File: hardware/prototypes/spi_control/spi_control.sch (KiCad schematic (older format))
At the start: 84 parts, among them J1 USB_B_Micro, J39 Versa_1, J40 Versa_2, U1 ST1L08SPU33R, U2 MCP2210-I_MQ, U3 ADAR7251, U4 BGT24_Module, Y1 12MHZ, Y2 40MHz

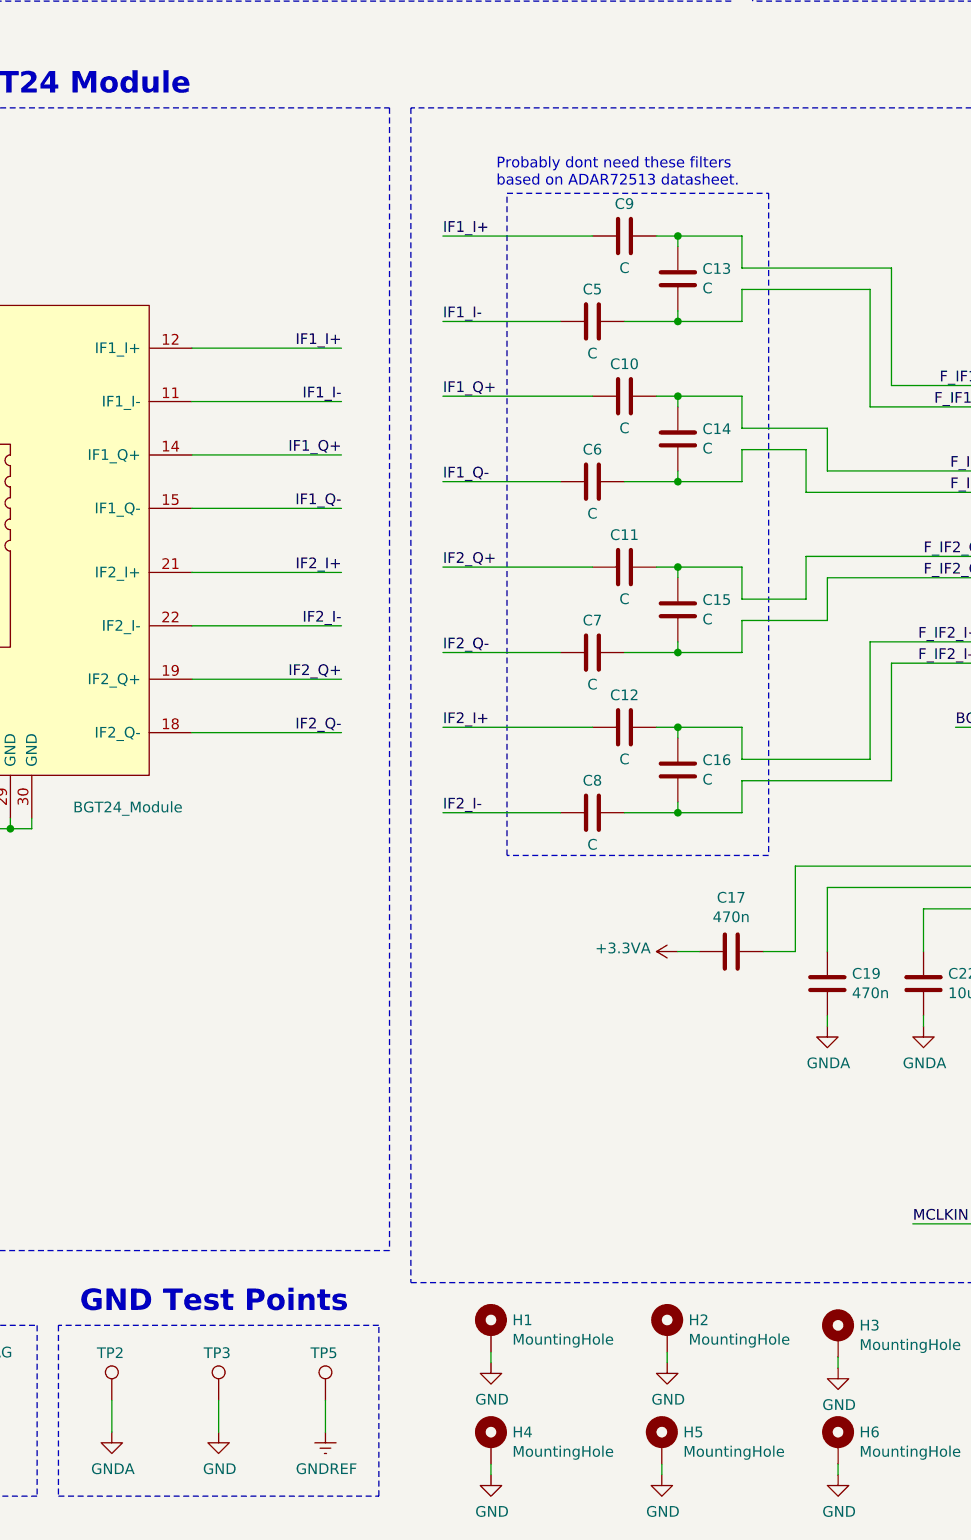
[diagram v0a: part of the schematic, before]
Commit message: Added Keystone GND probe point.
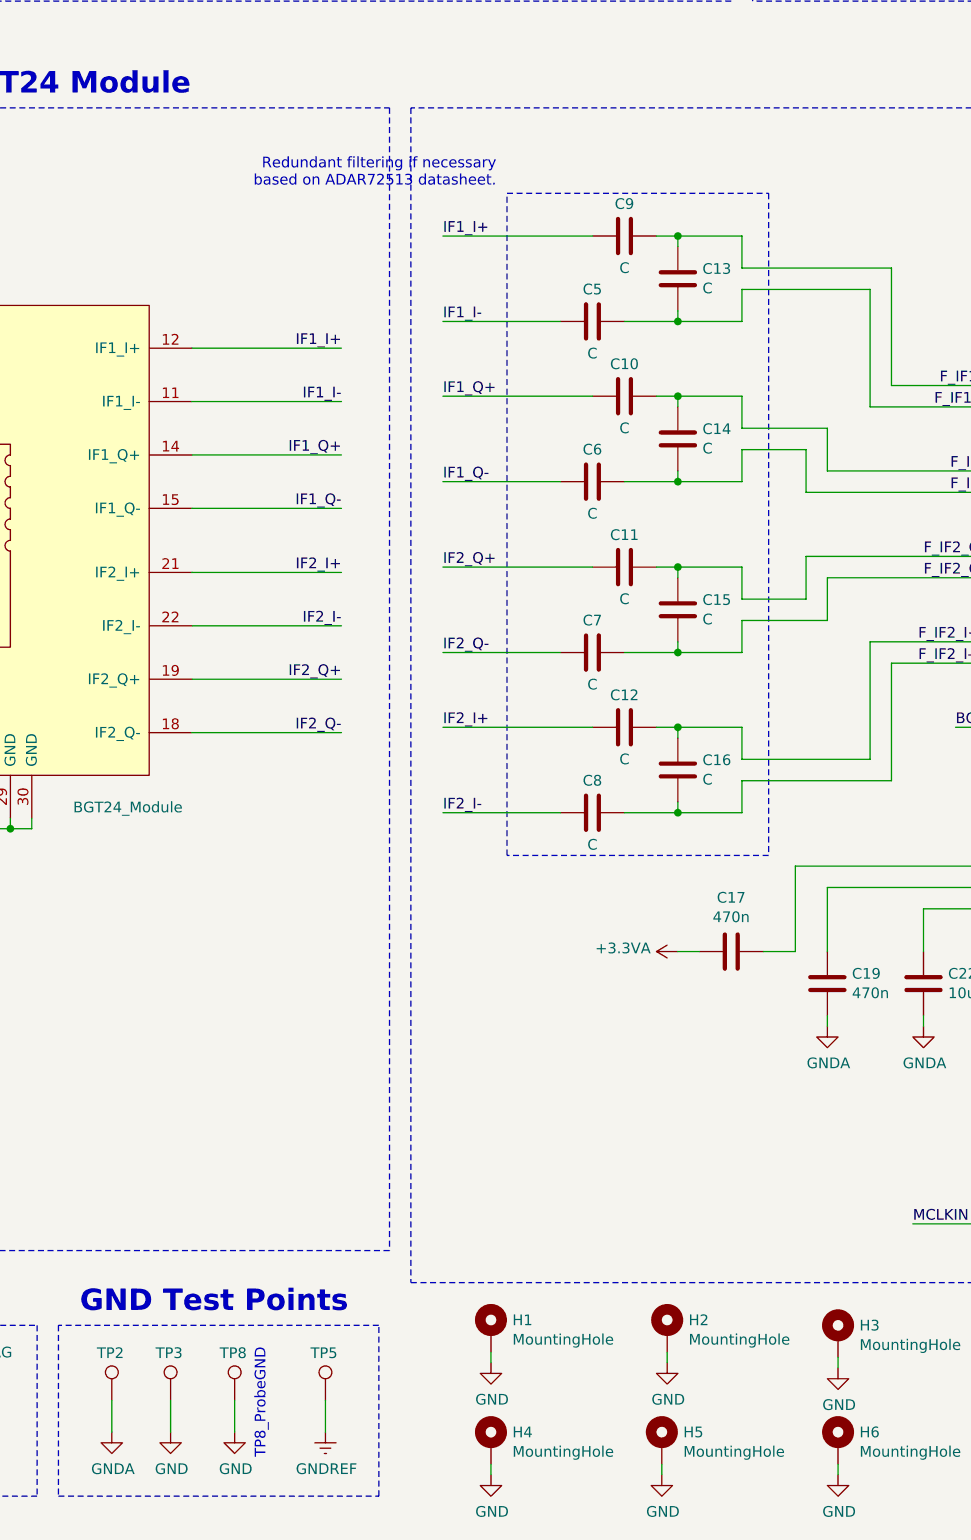
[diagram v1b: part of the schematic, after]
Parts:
- added TP8: TestPoint, TestPoint:TestPoint_Keystone_5019_Minature, symbol Connector:TestPoint
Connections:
- net GND: now also TP8.1
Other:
- note added: "Redundant filtering if necessary\nbased on ADAR72513 datasheet."
- note added: "TP8_ProbeGND"
- note removed: "Probably dont need these filters \nbased on ADAR72513 datasheet."
- moved on the sheet: TP3
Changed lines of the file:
@@
 L Connector:TestPoint TP3
 U 1 1 5E6578F5
-P 4100 9900
-F 0 "TP3" H 4030 10120 50  0000 L CNN
-F 1 "TestPoint" H 4158 9927 50  0001 L CNN
-F 2 "TestPoint:TestPoint_Pad_D1.0mm" H 4300 9900 50  0001 C CNN
-F 3 "~" H 4300 9900 50  0001 C CNN
-	1    4100 9900
+P 3875 9900
+F 0 "TP3" H 3805 10120 50  0000 L CNN
+F 1 "TestPoint" H 3933 9927 50  0001 L CNN
+F 2 "TestPoint:TestPoint_Pad_D1.0mm" H 4075 9900 50  0001 C CNN
+F 3 "~" H 4075 9900 50  0001 C CNN
+	1    3875 9900
 	1    0    0    -1
 $EndComp
@@
 L power:GND #PWR0142
 U 1 1 5E66375C
-P 4100 10050
-F 0 "#PWR0142" H 4100 9800 50  0001 C CNN
-F 1 "GND" H 4105 9877 50  0000 C CNN
-F 2 "" H 4100 10050 50  0001 C CNN
-F 3 "" H 4100 10050 50  0001 C CNN
-	1    4100 10050
+P 3875 10050
+F 0 "#PWR0142" H 3875 9800 50  0001 C CNN
+F 1 "GND" H 3880 9877 50  0000 C CNN
+F 2 "" H 3875 10050 50  0001 C CNN
+F 3 "" H 3875 10050 50  0001 C CNN
+	1    3875 10050
 	1    0    0    -1
 $EndComp
@@
 	4600 10050 4600 9900
 Wire Wire Line
-	4100 9900 4100 10050
+	3875 9900 3875 10050
 Wire Wire Line
 	3600 9900 3600 10050
@@
 Wire Notes Line
 	6675 4250 6675 7350
-Text Notes 5400 4225 0    50   ~ 0
-Probably dont need these filters \nbased on ADAR72513 datasheet.
+Text Notes 5400 4225 2    50   ~ 0
+Redundant filtering if necessary\nbased on ADAR72513 datasheet.
 Text Label 4675 6275 2    50   ~ 0
 IF2_I-
@@
 Wire Notes Line
 	5450 4250 6675 4250
+$Comp
+L Connector:TestPoint TP8
+U 1 1 5EA8B203
+P 4175 9900
+F 0 "TP8" H 4105 10120 50  0000 L CNN
+F 1 "TestPoint" H 4233 9927 50  0001 L CNN
+F 2 "TestPoint:TestPoint_Keystone_5019_Minature" H 4375 9900 50  0001 C CNN
+F 3 "~" H 4375 9900 50  0001 C CNN
+	1    4175 9900
+	1    0    0    -1
+$EndComp
+$Comp
+L power:GND #PWR?
+U 1 1 5EA8B209
+P 4175 10050
+F 0 "#PWR?" H 4175 9800 50  0001 C CNN
+F 1 "GND" H 4180 9877 50  0000 C CNN
+F 2 "" H 4175 10050 50  0001 C CNN
+F 3 "" H 4175 10050 50  0001 C CNN
+	1    4175 10050
+	1    0    0    -1
+$EndComp
+Wire Wire Line
+	4175 9900 4175 10050
+Text Notes 4325 10175 1    50   ~ 0
+TP8_ProbeGND
 $EndSCHEMATC

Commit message: Resolve 4, 11, 16, 18, and 25 from #24 and includes misc. improvements
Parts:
- added M1, M2, M3, M4, M5, M6: STANDOFF, symbol bloop:STANDOFF
- C10, C11, C12, C13, C14, C15, C16, C5, C6, C7, C8, C9: value C -> TBD
- H1, H2, H3, H4, H5, H6: value MountingHole -> MNT_HOLE
- renumbered C21 to C18, C18 to C19, C19 to C20, C20 to C21, FB2 to FB1, FB1 to FB2, J40 to J2, J39 to J3, TP8 to TP4, TP4 to TP6, TP6 to TP7, TP7 to TP8, U4 to U1, U1 to U2, U2 to U3, U3 to U4
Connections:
- net GND: now also J1.5 (GND)
- net GNDREF: no longer J1.5 (GND)
- no-connect marks 35 -> 36
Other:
- note added: "32 mA (typ)"
- note added: "M2 Standoffs"
- note added: "Mounting Holes"
- note added: "Radar MMIC - BGT24 Module"
- note removed: "RF Transceiver - BGT24 Module"
- moved on the sheet: C18, C23, C25, C26, H1, H2, H3, H4, H5, H6, R5, R6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

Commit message: Resolve 9 from #24; added some vias to layout and moved a few tracks
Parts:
- Y2: footprint Oscillator:Oscillator_SMD_Abracon_ASE-4Pin_3.2x2.5mm -> Crystal:Crystal_SMD_Abracon_ABM8G-4Pin_3.2x2.5mm
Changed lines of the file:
@@
 Wire Wire Line
 	1450 1500 2050 1500
-$Comp
-L Device:Crystal_GND24 Y1
-U 1 1 5FC6E4E6
-P 7300 2500
-F 0 "Y1" H 7400 2275 50  0000 L CNN
-F 1 "12MHZ" H 6900 2650 50  0000 L CNN
-F 2 "Crystal:Crystal_SMD_Abracon_ABM8G-4Pin_3.2x2.5mm" H 7300 2500 50  0001 C CNN
-F 3 "https://ecsxtal.com/store/pdf/ecx-32.pdf" H 7300 2500 50  0001 C CNN
-F 4 "ECS-120-12-33-AGN-TR" H 7300 2500 50  0001 C CNN "MPN"
-	1    7300 2500
-	1    0    0    -1
-$EndComp
 Connection ~ 9275 8350
 Wire Wire Line
@@
 F 0 "Y2" V 9100 8475 50  0000 L CNN
 F 1 "40MHz" V 9100 8700 50  0000 L CNN
-F 2 "Oscillator:Oscillator_SMD_Abracon_ASE-4Pin_3.2x2.5mm" H 9275 8625 50  0001 C CNN
+F 2 "Crystal:Crystal_SMD_Abracon_ABM8G-4Pin_3.2x2.5mm" H 9275 8625 50  0001 C CNN
 F 3 "https://ecsxtal.com/store/pdf/ecx-32.pdf" H 9275 8625 50  0001 C CNN
 F 4 "ECS-400-18-33-JGN-TR" H 9275 8625 50  0001 C CNN "MPN"
@@
 Wire Wire Line
 	7250 1250 7250 1300
+$Comp
+L Device:Crystal_GND24 Y1
+U 1 1 5FC6E4E6
+P 7300 2500
+F 0 "Y1" H 7400 2275 50  0000 L CNN
+F 1 "12MHZ" H 6900 2650 50  0000 L CNN
+F 2 "Crystal:Crystal_SMD_Abracon_ABM8G-4Pin_3.2x2.5mm" H 7300 2500 50  0001 C CNN
+F 3 "https://ecsxtal.com/store/pdf/ecx-32.pdf" H 7300 2500 50  0001 C CNN
+F 4 "ECS-120-12-33-AGN-TR" H 7300 2500 50  0001 C CNN "MPN"
+	1    7300 2500
+	1    0    0    -1
+$EndComp
 $EndSCHEMATC

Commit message: Finalize BOM, finish schematic annotations, re-generate gerbers. Close #24
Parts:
- C1: Category (none) -> Passive; DK_Detail_Page (none) -> https://www.digikey.com/product-detail/en/murata-electronic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; Description (none) -> CAP CER 100PF 50V C0G/NP0 0402; Digi-Key_PN (none) -> 490-10669-1-ND; Family (none) -> Ceramic Capacitors; MPN (none) -> GCM1555C1H101JA16D; Manufacturer (none) -> Murata Electronics; Status (none) -> Active
- C10, C11, C12, C13, C14, C15, C16, C5, C6, C7, C8, C9: Category (none) -> Passive
- C17, C20: Category (none) -> Passive; DK_Detail_Page (none) -> https://www.digikey.com/product-detail/en/samsung-electro-m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; Description (none) -> CAP CER 0.47UF 6.3V X5R 0402; Digi-Key_PN (none) -> 1276-1479-1-ND; Family (none) -> Ceramic Capacitors; MPN (none) -> CL05A474KQ5NNNC; Manufacturer (none) -> Samsung Electro-Mechanics; Status (none) -> Active
- C18, C23: Category (none) -> Passive; DK_Detail_Page (none) -> https://www.digikey.com/product-detail/en/kemet/C0402C120J5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; Description (none) -> CAP CER 12PF 50V C0G/NP0 0402; Digi-Key_PN (none) -> 399-1013-1-ND; Family (none) -> Ceramic Capacitors; MPN (none) -> C0402C120J5GACTU; Manufacturer (none) -> KEMET; Status (none) -> Active
- C19, C3: Category (none) -> Passive; DK_Detail_Page (none) -> https://www.digikey.com/product-detail/en/samsung-electro-m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; Description (none) -> CAP CER 1UF 6.3V X5R 0402; Digi-Key_PN (none) -> 1276-1235-1-ND; Family (none) -> Ceramic Capacitors; MPN (none) -> CL05A105MQ5NNNC; Manufacturer (none) -> Samsung Electro-Mechanics; Status (none) -> Active
- C2, C4: Category (none) -> Passive; DK_Detail_Page (none) -> https://www.digikey.com/product-detail/en/murata-electronic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; Description (none) -> CAP CER 4.7UF 6.3V X5R 0402; Digi-Key_PN (none) -> 490-5915-1-ND; Family (none) -> Ceramic Capacitors; MPN (none) -> GRM155R60J475ME47D; Manufacturer (none) -> Murata Electronics; Status (none) -> Active
- C21, C24, C33, C37, C38, C39, C40, C41, C42, C43: Category (none) -> Passive; DK_Detail_Page (none) -> https://www.digikey.com/product-detail/en/samsung-electro-m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; Description (none) -> CAP CER 0.1UF 6.3V X5R 0402; Digi-Key_PN (none) -> 1276-1442-1-ND; Family (none) -> Ceramic Capacitors; MPN (none) -> CL05A104KQ5NNNC; Manufacturer (none) -> Samsung Electro-Mechanics; Status (none) -> Active
- C22, C28, C30, C31, C32, C34, C35, C36: Category (none) -> Passive; DK_Detail_Page (none) -> https://www.digikey.com/product-detail/en/murata-electronic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; Description (none) -> CAP CER 10UF 6.3V X6S 0402; Digi-Key_PN (none) -> 490-13233-1-ND; Family (none) -> Ceramic Capacitors; MPN (none) -> GRM155C80J106ME11D; Manufacturer (none) -> Murata Electronics; Status (none) -> Active
- C25, C26: Category (none) -> Passive; DK_Detail_Page (none) -> https://www.digikey.com/product-detail/en/avx-corporation/0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; Description (none) -> CAP CER 18PF 50V C0G/NP0 0402; Digi-Key_PN (none) -> 478-1073-1-ND; Family (none) -> Ceramic Capacitors; MPN (none) -> 04025A180JAT2A; Manufacturer (none) -> AVX Corporation; Status (none) -> Active
- C27: Category (none) -> Passive; DK_Detail_Page (none) -> https://www.digikey.com/product-detail/en/samsung-electro-m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; Description (none) -> CAP CER 5600PF 25V X7R 0402; Digi-Key_PN (none) -> 1276-1578-1-ND; Family (none) -> Ceramic Capacitors; MPN (none) -> CL05B562KA5NNNC; Manufacturer (none) -> Samsung Electro-Mechanics; Status (none) -> Active
- C29: Category (none) -> Passive; DK_Detail_Page (none) -> https://www.digikey.com/product-detail/en/samsung-electro-m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; Description (none) -> CAP CER 390PF 50V X7R 0402; Digi-Key_PN (none) -> 1276-1560-1-ND; Family (none) -> Ceramic Capacitors; MPN (none) -> CL05B391KB5NNNC; Manufacturer (none) -> Samsung Electro-Mechanics; Status (none) -> Active
- C44: Category (none) -> Passive; DK_Detail_Page (none) -> https://www.digikey.com/product-detail/en/kemet/C0402C102K5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; Description (none) -> CAP CER 1000PF 50V X7R 0402; Digi-Key_PN (none) -> 399-1032-1-ND; Family (none) -> Ceramic Capacitors; MPN (none) -> C0402C102K5RACTU; Manufacturer (none) -> KEMET; Status (none) -> Active
- D1: DK_Datasheet_Link https://www.littelfuse.com/~/media/files/littelfuse/technic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 -> (none)
- D2: value GREEN_LED -> GRN; Category (none) -> LED Indication; DK_Detail_Page (none) -> https://www.digikey.com/product-detail/en/rohm-semiconducto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; Description (none) -> LED GREEN CLEAR 1006 SMD; Digi-Key_PN (none) -> 846-1197-1-ND; Family (none) -> LED Indication - Discrete; MPN (none) -> SML-P13PTT86R; Manufacturer (none) -> Rohm Semiconductor; Status (none) -> Active
- D3, D4: Category (none) -> LED Indication; DK_Detail_Page (none) -> https://www.digikey.com/product-detail/en/rohm-semiconducto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; Description (none) -> LED GREEN CLEAR 1006 SMD; Digi-Key_PN (none) -> 846-1197-1-ND; Family (none) -> LED Indication - Discrete; MPN (none) -> SML-P13PTT86R; Manufacturer (none) -> Rohm Semiconductor; Status (none) -> Active
- FB1, FB2: value Ferrite_Bead -> 1k; Category (none) -> Passive; DK_Detail_Page (none) -> https://www.digikey.com/product-detail/en/w-rth-elektronik/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; Description (none) -> FERRITE BEAD 1 KOHM 0603 1LN; Digi-Key_PN (none) -> 732-4670-1-ND; Family (none) -> FFerrite Beads and Chips; MPN (none) -> 742792662; Manufacturer (none) -> Würth Elektronik; Status (none) -> Active
- J1: Category (none) -> Connectors, Interconnects; DK_Detail_Page (none) -> https://www.digikey.com/product-detail/en/amphenol-icc-fci/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; Description (none) -> CONN RCPT USB2.0 MICRO B SMD R/A; Digi-Key_PN (none) -> 609-4616-1-ND; Family (none) -> USB, DVI, HDMI Connectors; MPN (none) -> 10118193-0001LF; Manufacturer (none) -> Amphenol ICC (FCI); Status (none) -> Active
- J2, J3: Category (none) -> Headers; DK_Detail_Page (none) -> https://www.digikey.com/product-detail/en/sullins-connector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; Description (none) -> CONN HDR 40POS 0.1 TIN SMD; Digi-Key_PN (none) -> S5690-ND; Family (none) -> Rectangular Connectors - Headers, Receptacles, Female Socke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; MPN (none) -> NPTC202KFMS-RC; Manufacturer (none) -> Sullins Connector Solutions; Status (none) -> Active
- M1, M2, M3, M4, M5, M6: Category (none) -> Hardware
- R1: Category (none) -> Passive; DK_Detail_Page (none) -> https://www.digikey.com/product-detail/en/yageo/RC0402FR-07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; Description (none) -> RES SMD 1M OHM 1% 1/16W 0402; Digi-Key_PN (none) -> 311-1.00MLRCT-ND; Family (none) -> Chip Resistor - SMT; MPN (none) -> RC0402FR-071ML; Manufacturer (none) -> Yageo; Status (none) -> Active
- R10, R4: Category (none) -> Passive; DK_Detail_Page (none) -> https://www.digikey.com/product-detail/en/yageo/RC0402FR-07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; Description (none) -> RES SMD 1K OHM 1% 1/16W 0402; Digi-Key_PN (none) -> 311-1.00KLRCT-ND; Family (none) -> Chip Resistor - SMT; MPN (none) -> RC0402FR-071KL; Manufacturer (none) -> Yageo; Status (none) -> Active
- R11, R12, R9: Category (none) -> Passive; DK_Detail_Page (none) -> https://www.digikey.com/product-detail/en/yageo/RC0402FR-07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; Description (none) -> RES SMD 10K OHM 1% 1/16W 0402; Digi-Key_PN (none) -> 311-10.0KLRCT-ND; Family (none) -> Chip Resistor - SMT; MPN (none) -> RC0402FR-0710KL; Manufacturer (none) -> Yageo; Status (none) -> Active
- R2: Category (none) -> Passive; DK_Detail_Page (none) -> https://www.digikey.com/product-detail/en/yageo/RC0402JR-07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; Description (none) -> RES SMD 820 OHM 5% 1/16W 0402; Digi-Key_PN (none) -> 311-820JRCT-ND; Family (none) -> Chip Resistor - SMT; MPN (none) -> RC0402JR-07820RL; Manufacturer (none) -> Yageo; Status (none) -> Active
- R3, R8: Category (none) -> Passive; DK_Detail_Page (none) -> https://www.digikey.com/product-detail/en/yageo/RC0402FR-07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; Description (none) -> RES SMD 330 OHM 1% 1/16W 0402; Digi-Key_PN (none) -> 311-330LRCT-ND; Family (none) -> Chip Resistor - SMT; MPN (none) -> RC0402FR-07330RL; Manufacturer (none) -> Yageo; Status (none) -> Active
- R5, R6, R7: Category (none) -> Passive; DK_Detail_Page (none) -> https://www.digikey.com/product-detail/en/yageo/RC0402JR-07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; Description (none) -> RES SMD 0 OHM JUMPER 1/16W 0402; Digi-Key_PN (none) -> 311-0.0JRCT-ND; Family (none) -> Chip Resistor - SMT; MPN (none) -> RC0402JR-070RL; Manufacturer (none) -> Yageo; Status (none) -> Active
- TP4: Category (none) -> Test and Measurement; DK_Detail_Page (none) -> https://www.digikey.com/product-detail/en/keystone-electron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; Description (none) -> PC TEST POINT MINIATURE; Digi-Key_PN (none) -> 36-5019CT-ND; Family (none) -> Test Points; MPN (none) -> 5019; Manufacturer (none) -> Keystone Electronics; Status (none) -> Active
- U1: Category (none) -> Radar Module
- U2: Category (none) -> Active; DK_Detail_Page (none) -> https://www.digikey.com/product-detail/en/stmicroelectronic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; Description (none) -> IC REG LINEAR 3.3V 800MA 8DFN; Digi-Key_PN (none) -> 497-15508-1-ND; Family (none) -> PMIC - Voltage Regulators - Linear; Manufacturer (none) -> STMicroelectronics; Status (none) -> Active
- U3: Category (none) -> Active; DK_Detail_Page (none) -> https://www.digikey.com/product-detail/en/microchip-technol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; Description (none) -> IC CONVERTER USB-SPI 20-QFN; Digi-Key_PN (none) -> MCP2210-I/MQ-ND; Family (none) -> Interface - Controllers; MPN (none) -> MCP2210-I/MQ; Manufacturer (none) -> Microchip Technology; Status (none) -> Active
- U4: Category (none) -> Active; DK_Detail_Page (none) -> https://www.digikey.com/product-detail/en/analog-devices-in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; Description (none) -> IC ADC 16BIT SIGMA-DELTA 48LFCSP; Digi-Key_PN (none) -> ADAR7251WBCSZ-ND; Family (none) -> Data Acquisition - ADC; MPN (none) -> ADAR7251WBCSZ; Manufacturer (none) -> Analog Devices Inc.; Status (none) -> Active
- Y1: Category (none) -> Crystal; DK_Detail_Page (none) -> https://www.digikey.com/product-detail/en/ecs-inc/ECS-120-1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; Description (none) -> CRYSTAL 12MHZ 12PF SMD; Digi-Key_PN (none) -> XC2611CT-ND; Family (none) -> Crystals; Manufacturer (none) -> ECS Inc.; Status (none) -> Active
- Y2: Category (none) -> Crystal; DK_Detail_Page (none) -> https://www.digikey.com/product-detail/en/ecs-inc/ECS-400-1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; Description (none) -> CRYSTAL 40MHZ 18PF SMD; Digi-Key_PN (none) -> XC2717CT-ND; Family (none) -> Crystals; Manufacturer (none) -> ECS Inc.; Status (none) -> Active
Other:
- note added: "+3.3V @ 800 mA"
- note added: "270 mA (max)"
- note added: "To ECP5\nEval J39"
- note added: "To ECP5\nEval J40"
